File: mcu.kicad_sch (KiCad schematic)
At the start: 11 parts, among them J1 Boot Opt, J2 UART Debug, J3 GPIO Debug, J4 Signals Debug, SW1 Reset, U1 ESP32-S3-WROOM-1-N8

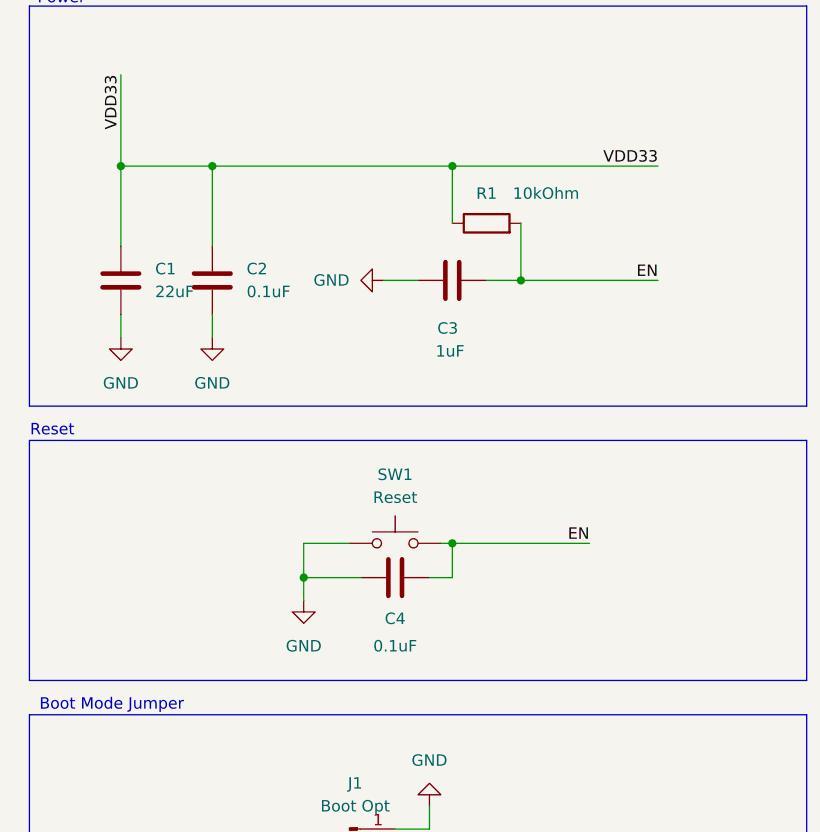
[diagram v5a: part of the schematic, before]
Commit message: Changed the default symbols with JLC's one
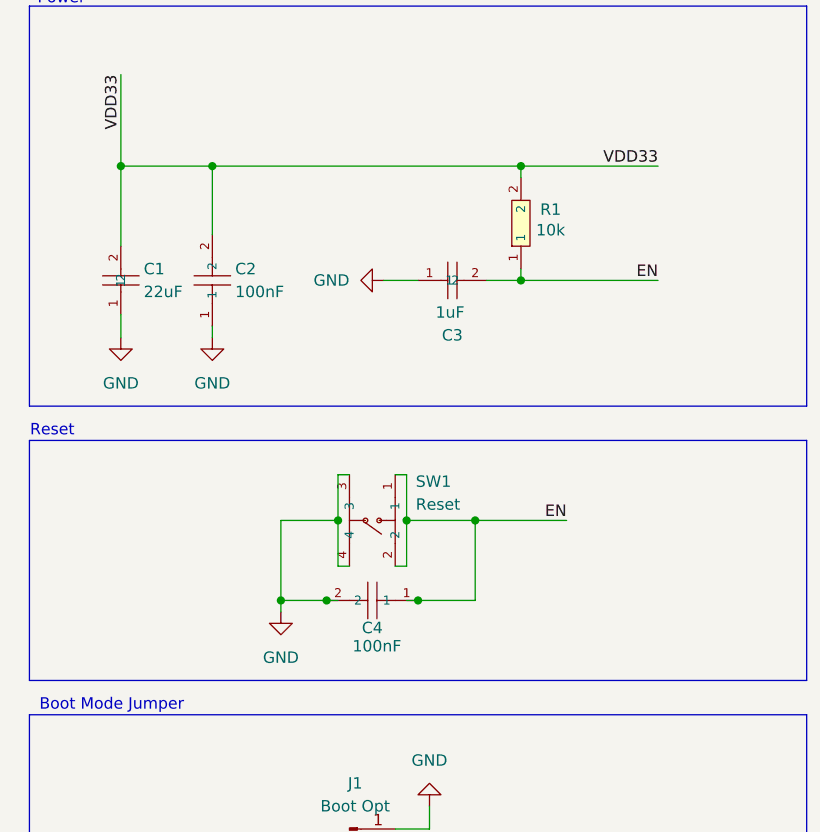
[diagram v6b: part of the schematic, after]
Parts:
- C1: footprint (none) -> lcsc_footprints:C1859_C1206; symbol Device:C -> lcsc_imported:22uF_(226)_±10%_10V; LCSC (none) -> C1859; Manufacturer (none) -> FH(风华)
- C2, C4: value 0.1uF -> 100nF; footprint (none) -> lcsc_footprints:C1525_C0402; symbol Device:C -> lcsc_imported:100nF_(104)_±10%_16V; LCSC (none) -> C1525; Manufacturer (none) -> SAMSUNG(三星)
- C3: footprint (none) -> lcsc_footprints:C1592_C0603; symbol Device:C -> lcsc_imported:1uF_(105)_±10%_16V; LCSC (none) -> C1592; Manufacturer (none) -> SAMSUNG(三星)
- R1: value 10kOhm -> 10k; footprint (none) -> lcsc_footprints:C1489_R1206; symbol Device:R -> lcsc_imported:10KΩ_(103)_±5%; LCSC (none) -> C1489; Manufacturer (none) -> UNI-ROYAL(厚声)
- SW1: footprint (none) -> lcsc_footprints:C55200589_SW-SMD_4P-L4_2-W3_4-P2_15-LS5_2; symbol Switch:SW_Push -> lcsc_imported:HX_3X4X2_5-PA-4N_PUSH_BUTTON_SWITCH; LCSC (none) -> C55200589; Manufacturer (none) -> hanxia(韩下)
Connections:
- net EN: now also C3.2, C4.1, R1.1, SW1.1; no longer C3.1, C4.2, R1.2
- net GND: now also C1.1, C2.1, C3.1, C4.2, SW1.3, SW1.4; no longer C1.2, C2.2, C3.2, C4.1, SW1.1
- net VDD: now also C1.2, C2.2, R1.2; no longer C1.1, C2.1, R1.1

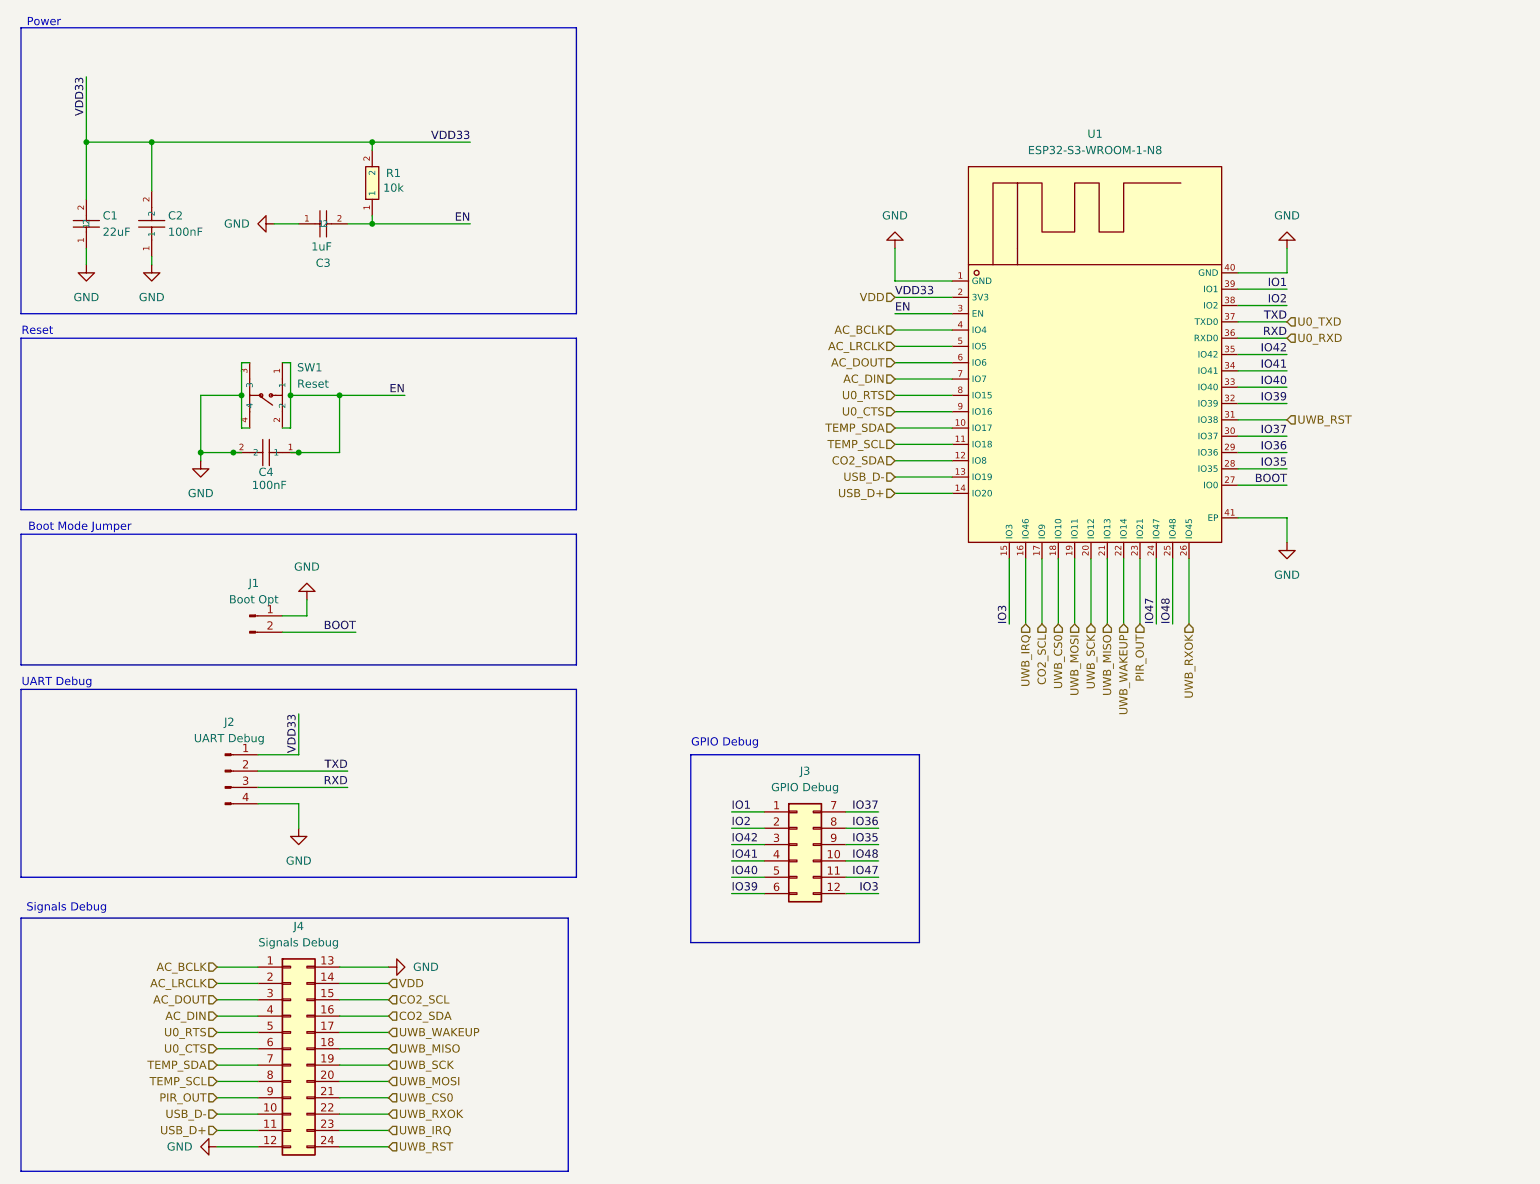
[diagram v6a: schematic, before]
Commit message: Changed footprint of the test point
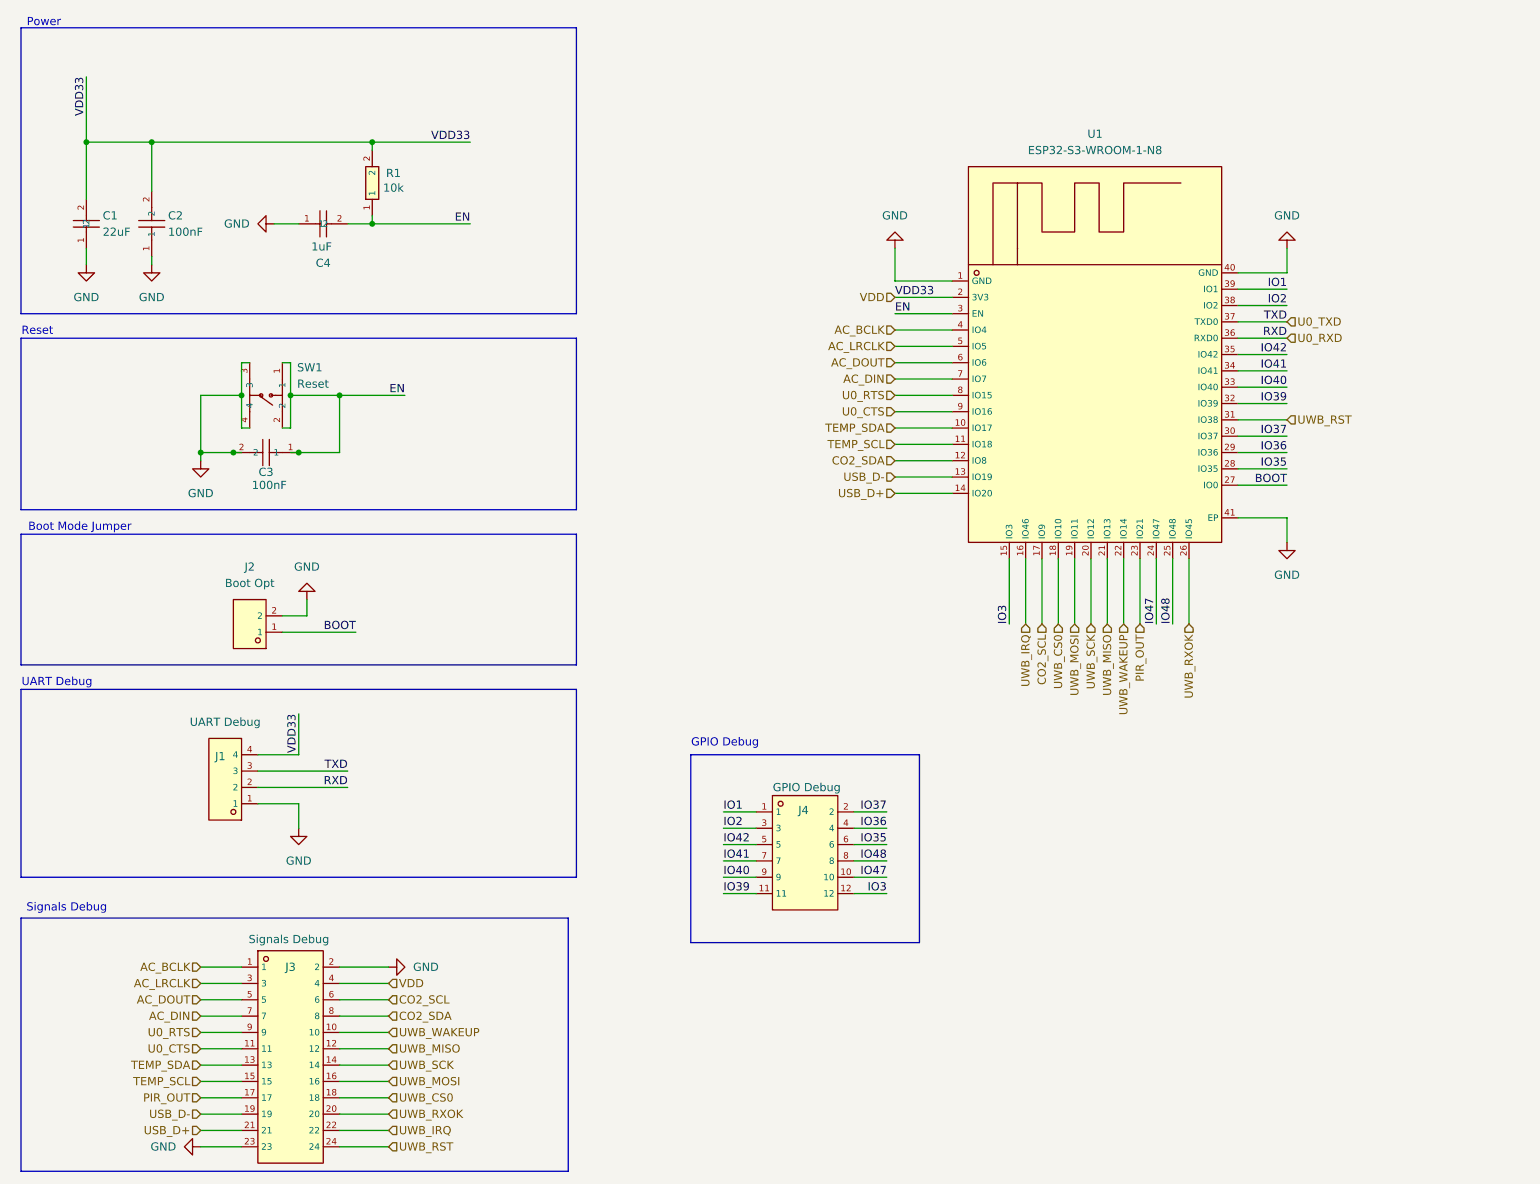
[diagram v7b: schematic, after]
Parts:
- J1: renamed from J2; footprint (none) -> Connector_PinHeader_1.27mm:PinHeader_1x04_P1.27mm_Vertical_SMD_Pin1Left; symbol Connector:Conn_01x04_Pin -> lcsc_imported:HX_PZ1_27-1X4P_ZZ; LCSC (none) -> C22438101; Manufacturer (none) -> hanxia(韩下)
- J2: renamed from J1; footprint (none) -> Connector_PinHeader_1.27mm:PinHeader_1x02_P1.27mm_Vertical_SMD_Pin1Left; symbol Connector:Conn_01x02_Pin -> lcsc_imported:1_27MM/1*2P; LCSC (none) -> C703015; Manufacturer (none) -> BOOMELE(博穆精密)
- J3: renamed from J4; footprint (none) -> Connector_PinHeader_1.27mm:PinHeader_2x12_P1.27mm_Vertical_SMD; symbol Connector_Generic:Conn_02x12_Top_Bottom -> lcsc_imported:1271WV-2X12P; LCSC (none) -> C7470094; Manufacturer (none) -> HanElectricity(瀚源)
- J4: renamed from J3; footprint (none) -> Connector_PinHeader_1.27mm:PinHeader_2x06_P1.27mm_Vertical_SMD; symbol Connector_Generic:Conn_02x06_Top_Bottom -> lcsc_imported:1271WV-2X6P; LCSC (none) -> C7470091; Manufacturer (none) -> HanElectricity(瀚源)
- renumbered C4 to C3, C3 to C4
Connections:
- net AC_DIN: now also J3.7; no longer J3.4 (Pin_4)
- net AC_DOUT: now also J3.5; no longer J3.3 (Pin_3)
- net AC_LRCLK: now also J3.3; no longer J3.2 (Pin_2)
- net BOOT: now also J2.1; no longer J2.2 (Pin_2)
- net CO2_SCL: now also J3.6; no longer J3.15 (Pin_15)
- net CO2_SDA: now also J3.8; no longer J3.16 (Pin_16)
- net GND: now also J1.1, J2.2, J3.2, J3.23; no longer J1.4 (Pin_4), J2.1 (Pin_1), J3.12 (Pin_12), J3.13 (Pin_13)
- net IO2: now also J4.3; no longer J4.2 (Pin_2)
- net IO35: now also J4.6; no longer J4.9 (Pin_9)
- net IO36: now also J4.4; no longer J4.8 (Pin_8)
- net IO37: now also J4.2; no longer J4.7 (Pin_7)
- net IO39: now also J4.11; no longer J4.6 (Pin_6)
- net IO40: now also J4.9; no longer J4.5 (Pin_5)
- net IO41: now also J4.7; no longer J4.4 (Pin_4)
- net IO42: now also J4.5; no longer J4.3 (Pin_3)
- net IO47: now also J4.10; no longer J4.11 (Pin_11)
- net IO48: now also J4.8; no longer J4.10 (Pin_10)
- net PIR_OUT: now also J3.17; no longer J3.9 (Pin_9)
- net TEMP_SCL: now also J3.15; no longer J3.8 (Pin_8)
- net TEMP_SDA: now also J3.13; no longer J3.7 (Pin_7)
- net U0_CTS: now also J3.11; no longer J3.6 (Pin_6)
- net U0_RTS: now also J3.9; no longer J3.5 (Pin_5)
- net U0_RXD: now also J1.2; no longer J1.3 (Pin_3)
- net U0_TXD: now also J1.3; no longer J1.2 (Pin_2)
- net USB_D+: now also J3.21; no longer J3.11 (Pin_11)
- net USB_D-: now also J3.19; no longer J3.10 (Pin_10)
- net UWB_CS0: now also J3.18; no longer J3.21 (Pin_21)
- net UWB_IRQ: now also J3.22; no longer J3.23 (Pin_23)
- net UWB_MISO: now also J3.12; no longer J3.18 (Pin_18)
- net UWB_MOSI: now also J3.16; no longer J3.20 (Pin_20)
- net UWB_RXOK: now also J3.20; no longer J3.22 (Pin_22)
- net UWB_SCK: now also J3.14; no longer J3.19 (Pin_19)
- net UWB_WAKEUP: now also J3.10; no longer J3.17 (Pin_17)
- net VDD: now also J1.4, J3.4; no longer J1.1 (Pin_1), J3.14 (Pin_14)
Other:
- moved on the sheet: J2

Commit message: Data lines layout. Missing power lines and UWB
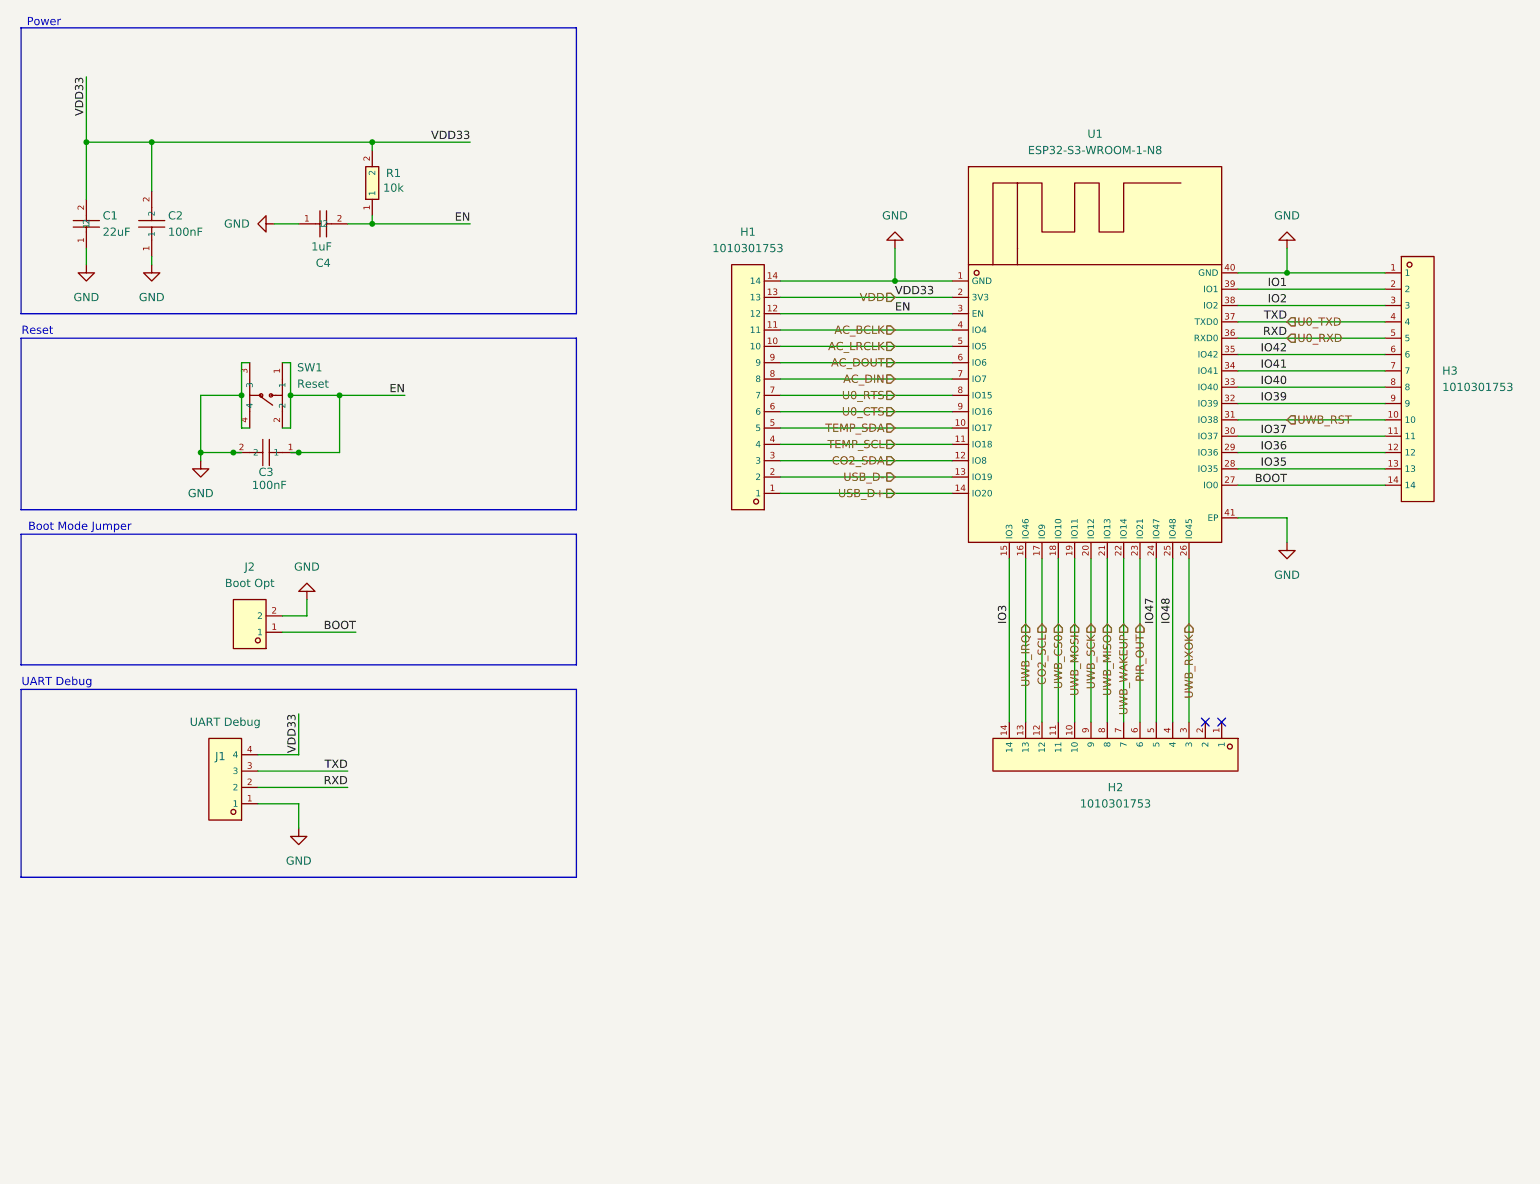
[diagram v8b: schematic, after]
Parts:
- removed J3: Signals Debug, Connector_PinHeader_1.27mm:PinHeader_2x12_P1.27mm_Vertical_SMD, symbol lcsc_imported:1271WV-2X12P
- removed J4: GPIO Debug, Connector_PinHeader_1.27mm:PinHeader_2x06_P1.27mm_Vertical_SMD, symbol lcsc_imported:1271WV-2X6P
- added H1, H2, H3: 1010301753, lcsc_footprints:C52016809_HDR-SMD_14P-P2_54-V-M-S4_8, symbol lcsc_imported:1010301753
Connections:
- net AC_BCLK: now also H1.11
- net AC_DIN: now also H1.8
- net AC_DOUT: now also H1.9
- net AC_LRCLK: now also H1.10
- net BOOT: now also H3.14
- net CO2_SCL: now also H2.12
- net CO2_SDA: now also H1.3
- net EN: now also H1.12
- net GND: now also H1.14, H3.1
- net IO1: now also H3.2
- net IO2: now also H3.3
- net IO3: now also H2.14
- net IO35: now also H3.13
- net IO36: now also H3.12
- net IO37: now also H3.11
- net IO39: now also H3.9
- net IO40: now also H3.8
- net IO41: now also H3.7
- net IO42: now also H3.6
- net IO47: now also H2.5
- net IO48: now also H2.4
- net PIR_OUT: now also H2.6
- net TEMP_SCL: now also H1.4
- net TEMP_SDA: now also H1.5
- net U0_CTS: now also H1.6
- net U0_RTS: now also H1.7
- net U0_RXD: now also H3.5
- net U0_TXD: now also H3.4
- net USB_D+: now also H1.1
- net USB_D-: now also H1.2
- net UWB_CS0: now also H2.11
- net UWB_IRQ: now also H2.13
- net UWB_MISO: now also H2.8
- net UWB_MOSI: now also H2.10
- net UWB_RST: now also H3.10
- net UWB_RXOK: now also H2.3
- net UWB_SCK: now also H2.9
- net UWB_WAKEUP: now also H2.7
- net VDD: now also H1.13
- no-connect marks 0 -> 2
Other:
- note removed: "GPIO Debug"
- note removed: "Signals Debug"
